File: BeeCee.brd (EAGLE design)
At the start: 100 x 80 mm, 7 parts

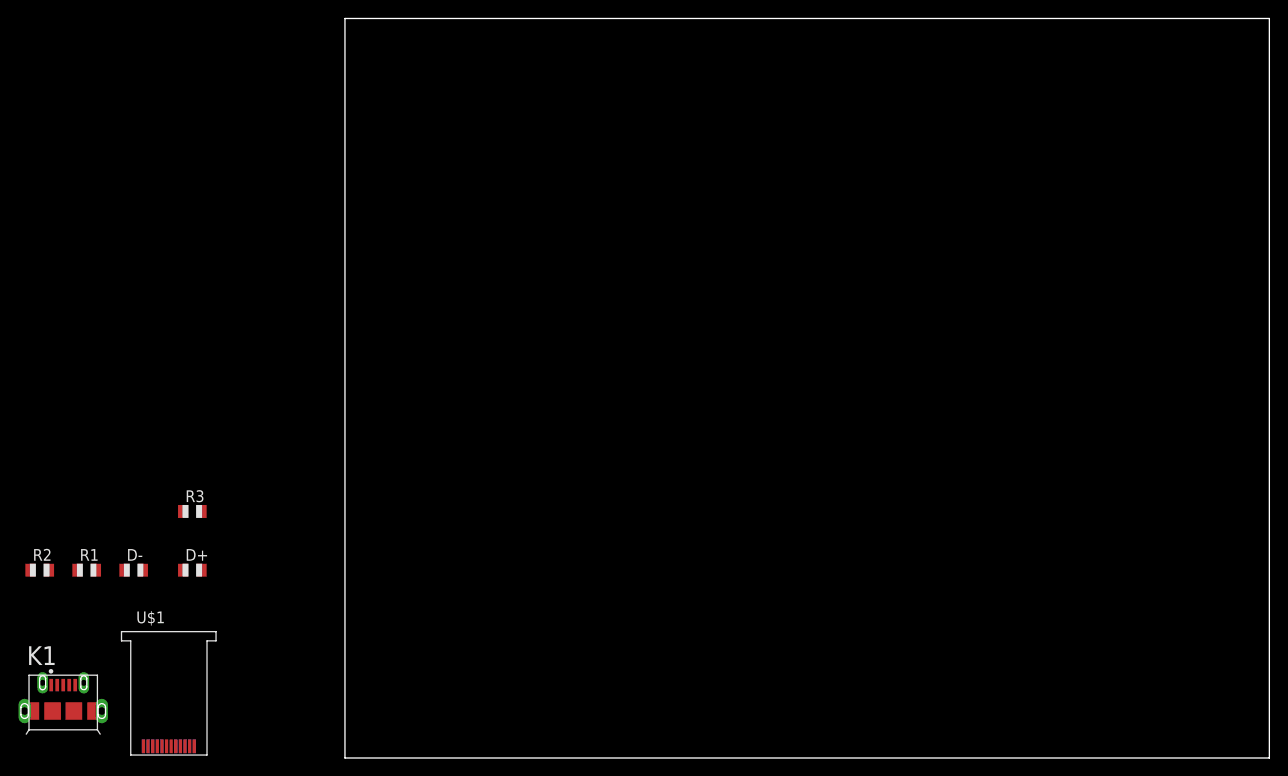
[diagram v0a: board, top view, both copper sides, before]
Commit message: preliminary component layout. Might be able to squeeze in a selector switch
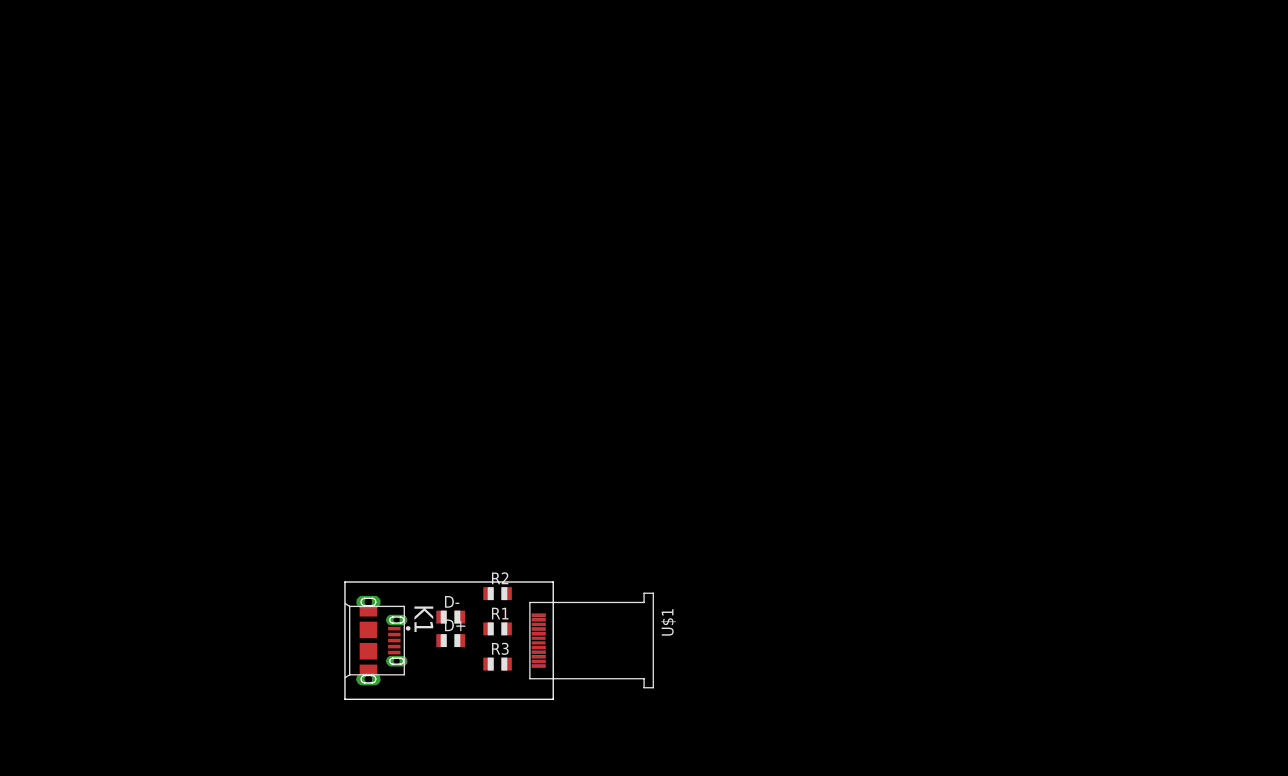
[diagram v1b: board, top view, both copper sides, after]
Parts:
- moved R2 49.6 mm to (16.5, 17.8)
- moved R1 44.9 mm to (16.5, 14.0)
- moved U$1 41.6 mm to (21.0, 12.7), turned to 270 degrees
- moved R3 36.9 mm to (16.5, 10.2)
- moved D- 34.7 mm to (11.4, 15.2)
- moved K1 33.9 mm to (2.54, 12.7), turned to 270 degrees
- moved D+ 29.0 mm to (11.4, 12.7)
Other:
- board size 100 x 80 mm -> 22.5 x 12.7 mm
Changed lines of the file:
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@@
 <board>
 <plain>
-<wire x1="0" y1="0" x2="100" y2="0" width="0" layer="20"/>
-<wire x1="100" y1="0" x2="100" y2="80" width="0" layer="20"/>
-<wire x1="100" y1="80" x2="0" y2="80" width="0" layer="20"/>
-<wire x1="0" y1="80" x2="0" y2="0" width="0" layer="20"/>
+<wire x1="0" y1="6.35" x2="22.53" y2="6.35" width="0" layer="20"/>
+<wire x1="22.53" y1="6.35" x2="22.53" y2="19.04" width="0" layer="20"/>
+<wire x1="22.53" y1="19.04" x2="0" y2="19.04" width="0" layer="20"/>
+<wire x1="0" y1="19.04" x2="0" y2="6.35" width="0" layer="20"/>
+<dimension x1="0" y1="6.35" x2="22.53" y2="6.35" x3="11.265" y3="1.27" textsize="1.778" layer="1"/>
 </plain>
 <attributes>
@@
 </class>
 </classes>
-<designrules name="default">
+<designrules name="default *">
 <description language="de">&lt;b&gt;EAGLE Design Rules&lt;/b&gt;
 &lt;p&gt;
@@
 <param name="mtCopper" value="0.035mm 0.035mm 0.035mm 0.035mm 0.035mm 0.035mm 0.035mm 0.035mm 0.035mm 0.035mm 0.035mm 0.035mm 0.035mm 0.035mm 0.035mm 0.035mm"/>
 <param name="mtIsolate" value="1.5mm 0.15mm 0.2mm 0.15mm 0.2mm 0.15mm 0.2mm 0.15mm 0.2mm 0.15mm 0.2mm 0.15mm 0.2mm 0.15mm 0.2mm"/>
-<param name="mdWireWire" value="8mil"/>
-<param name="mdWirePad" value="8mil"/>
-<param name="mdWireVia" value="8mil"/>
-<param name="mdPadPad" value="8mil"/>
-<param name="mdPadVia" value="8mil"/>
-<param name="mdViaVia" value="8mil"/>
-<param name="mdSmdPad" value="8mil"/>
-<param name="mdSmdVia" value="8mil"/>
-<param name="mdSmdSmd" value="8mil"/>
+<param name="mdWireWire" value="6mil"/>
+<param name="mdWirePad" value="6mil"/>
+<param name="mdWireVia" value="6mil"/>
+<param name="mdPadPad" value="6mil"/>
+<param name="mdPadVia" value="6mil"/>
+<param name="mdViaVia" value="6mil"/>
+<param name="mdSmdPad" value="6mil"/>
+<param name="mdSmdVia" value="6mil"/>
+<param name="mdSmdSmd" value="6mil"/>
 <param name="mdViaViaSameLayer" value="8mil"/>
 <param name="mnLayersViaInSmd" value="2"/>
@@
 </autorouter>
 <elements>
-<element name="D+" library="adafruit" package="R0805" value="DNP" x="-16.51" y="20.32"/>
-<element name="D-" library="adafruit" package="R0805" value="DNP" x="-22.86" y="20.32"/>
-<element name="K1" library="Eagle_INPUT_OUTPUT_CONNECTORS_rev15d" package="629105150921" value="" x="-30.48" y="5.08"/>
-<element name="R1" library="adafruit" package="R0805" value="56k" x="-27.94" y="20.32"/>
-<element name="R2" library="adafruit" package="R0805" value="22k" x="-33.02" y="20.32"/>
-<element name="R3" library="adafruit" package="R0805" value="10k" x="-16.51" y="26.67"/>
-<element name="U$1" library="Eagle_INPUT_OUTPUT_CONNECTORS_rev15d" package="632712000011" value="" x="-19.05" y="1.27"/>
+<element name="D+" library="adafruit" package="R0805" value="DNP" x="11.43" y="12.7"/>
+<element name="D-" library="adafruit" package="R0805" value="DNP" x="11.43" y="15.24"/>
+<element name="K1" library="Eagle_INPUT_OUTPUT_CONNECTORS_rev15d" package="629105150921" value="" x="2.54" y="12.7" rot="R270"/>
+<element name="R1" library="adafruit" package="R0805" value="56k" x="16.51" y="13.97"/>
+<element name="R2" library="adafruit" package="R0805" value="22k" x="16.51" y="17.78"/>
+<element name="R3" library="adafruit" package="R0805" value="10k" x="16.51" y="10.16"/>
+<element name="U$1" library="Eagle_INPUT_OUTPUT_CONNECTORS_rev15d" package="632712000011" value="" x="20.955" y="12.7" rot="R270"/>
 </elements>
 <signals>
@@
 <contactref element="K1" pad="12"/>
 <contactref element="K1" pad="13"/>
-<wire x1="-34.1725" y1="5.08" x2="-34.655" y2="5.08" width="0" layer="19" extent="1-1"/>
-<wire x1="-31.63" y1="5.08" x2="-34.1725" y2="5.08" width="0" layer="19" extent="1-1"/>
-<wire x1="-29.33" y1="5.08" x2="-31.63" y2="5.08" width="0" layer="19" extent="1-1"/>
-<wire x1="-26.7875" y1="5.08" x2="-29.33" y2="5.08" width="0" layer="19" extent="1-1"/>
-<wire x1="-26.305" y1="5.08" x2="-26.7875" y2="5.08" width="0" layer="19" extent="1-1"/>
-<wire x1="-29.18" y1="7.885" x2="-29.33" y2="5.08" width="0" layer="19" extent="1-1"/>
-<wire x1="-28.255" y1="8.135" x2="-29.18" y2="7.885" width="0" layer="19" extent="1-1"/>
-<wire x1="-32.705" y1="8.135" x2="-31.63" y2="5.08" width="0" layer="19" extent="1-1"/>
-<wire x1="-21.8" y1="1.27" x2="-26.305" y2="5.08" width="0" layer="19" extent="1-1"/>
-<wire x1="-21.8" y1="1.27" x2="-21.8" y2="1.27" width="0" layer="19" extent="1-16"/>
-<wire x1="-16.3" y1="1.27" x2="-21.8" y2="1.27" width="0" layer="19" extent="1-1"/>
-<wire x1="-16.3" y1="1.27" x2="-16.3" y2="1.27" width="0" layer="19" extent="1-16"/>
+<wire x1="20.955" y1="15.45" x2="20.955" y2="15.45" width="0" layer="19" extent="1-16"/>
+<wire x1="20.955" y1="9.95" x2="20.955" y2="15.45" width="0" layer="19" extent="1-1"/>
+<wire x1="20.955" y1="9.95" x2="20.955" y2="9.95" width="0" layer="19" extent="1-16"/>
+<wire x1="5.595" y1="14.925" x2="20.955" y2="15.45" width="0" layer="19" extent="1-1"/>
+<wire x1="2.54" y1="13.85" x2="5.595" y2="14.925" width="0" layer="19" extent="1-1"/>
+<wire x1="2.54" y1="11.55" x2="2.54" y2="13.85" width="0" layer="19" extent="1-1"/>
+<wire x1="2.54" y1="16.3925" x2="2.54" y2="13.85" width="0" layer="19" extent="1-1"/>
+<wire x1="2.54" y1="16.875" x2="2.54" y2="16.3925" width="0" layer="19" extent="1-1"/>
+<wire x1="2.54" y1="9.0075" x2="2.54" y2="11.55" width="0" layer="19" extent="1-1"/>
+<wire x1="2.54" y1="8.525" x2="2.54" y2="9.0075" width="0" layer="19" extent="1-1"/>
+<wire x1="5.345" y1="11.4" x2="2.54" y2="11.55" width="0" layer="19" extent="1-1"/>
+<wire x1="5.595" y1="10.475" x2="5.345" y2="11.4" width="0" layer="19" extent="1-1"/>
 </signal>
 <signal name="VCC">
@@
 <contactref element="R2" pad="2"/>
 <contactref element="R3" pad="2"/>
-<wire x1="-32.02" y1="20.32" x2="-31.78" y2="7.885" width="0" layer="19" extent="1-1"/>
-<wire x1="-26.94" y1="20.32" x2="-32.02" y2="20.32" width="0" layer="19" extent="1-1"/>
-<wire x1="-15.51" y1="26.67" x2="-26.94" y2="20.32" width="0" layer="19" extent="1-1"/>
-<wire x1="-20.3" y1="1.27" x2="-31.78" y2="7.885" width="0" layer="19" extent="1-1"/>
-<wire x1="-20.3" y1="1.27" x2="-20.3" y2="1.27" width="0" layer="19" extent="1-16"/>
-<wire x1="-17.8" y1="1.27" x2="-20.3" y2="1.27" width="0" layer="19" extent="1-1"/>
-<wire x1="-17.8" y1="1.27" x2="-17.8" y2="1.27" width="0" layer="19" extent="1-16"/>
+<wire x1="20.955" y1="13.95" x2="20.955" y2="13.95" width="0" layer="19" extent="1-16"/>
+<wire x1="20.955" y1="11.45" x2="20.955" y2="13.95" width="0" layer="19" extent="1-1"/>
+<wire x1="20.955" y1="11.45" x2="20.955" y2="11.45" width="0" layer="19" extent="1-16"/>
+<wire x1="17.51" y1="13.97" x2="20.955" y2="13.95" width="0" layer="19" extent="1-1"/>
+<wire x1="17.51" y1="10.16" x2="20.955" y2="11.45" width="0" layer="19" extent="1-1"/>
+<wire x1="17.51" y1="17.78" x2="17.51" y2="13.97" width="0" layer="19" extent="1-1"/>
+<wire x1="5.345" y1="14" x2="17.51" y2="13.97" width="0" layer="19" extent="1-1"/>
 </signal>
 <signal name="CC">
@@
 <contactref element="R2" pad="1"/>
 <contactref element="R3" pad="1"/>
-<wire x1="-28.94" y1="20.32" x2="-18.3" y2="1.27" width="0" layer="19" extent="1-1"/>
-<wire x1="-34.02" y1="20.32" x2="-28.94" y2="20.32" width="0" layer="19" extent="1-1"/>
-<wire x1="-17.51" y1="26.67" x2="-28.94" y2="20.32" width="0" layer="19" extent="1-1"/>
+<wire x1="15.51" y1="13.97" x2="15.51" y2="17.78" width="0" layer="19" extent="1-1"/>
+<wire x1="15.51" y1="10.16" x2="15.51" y2="13.97" width="0" layer="19" extent="1-1"/>
+<wire x1="20.955" y1="11.95" x2="15.51" y2="10.16" width="0" layer="19" extent="1-1"/>
 </signal>
 <signal name="D-">
 <contactref element="K1" pad="2"/>
 <contactref element="D-" pad="2"/>
-<wire x1="-21.86" y1="20.32" x2="-31.13" y2="7.885" width="0" layer="19" extent="1-1"/>
+<wire x1="5.345" y1="13.35" x2="12.43" y2="15.24" width="0" layer="19" extent="1-1"/>
 </signal>
 <signal name="D+">
 <contactref element="K1" pad="3"/>
 <contactref element="D+" pad="2"/>
-<wire x1="-15.51" y1="20.32" x2="-30.48" y2="7.885" width="0" layer="19" extent="1-1"/>
+<wire x1="5.345" y1="12.7" x2="12.43" y2="12.7" width="0" layer="19" extent="1-1"/>
 </signal>
 <signal name="DN1">
 <contactref element="D-" pad="1"/>
 <contactref element="U$1" pad="A7"/>
-<wire x1="-23.86" y1="20.32" x2="-19.3" y2="1.27" width="0" layer="19" extent="1-1"/>
+<wire x1="10.43" y1="15.24" x2="20.955" y2="12.95" width="0" layer="19" extent="1-1"/>
 </signal>
 <signal name="DP1">
 <contactref element="D+" pad="1"/>
 <contactref element="U$1" pad="A6"/>
-<wire x1="-17.51" y1="20.32" x2="-18.8" y2="1.27" width="0" layer="19" extent="1-1"/>
+<wire x1="10.43" y1="12.7" x2="20.955" y2="12.45" width="0" layer="19" extent="1-1"/>
 </signal>
 </signals>
